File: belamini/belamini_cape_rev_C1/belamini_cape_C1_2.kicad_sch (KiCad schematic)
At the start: 39 parts, among them IC4 TLV320AIC3104, IC5 MIC5317, IC6 USBLC6-2SC6, J2 Conn_01x03, J3 Conn_01x03, J4 Conn_01x03, J5 USB_A, P1 Conn_02x18_Odd_Even, P2 Conn_02x18_Odd_Even

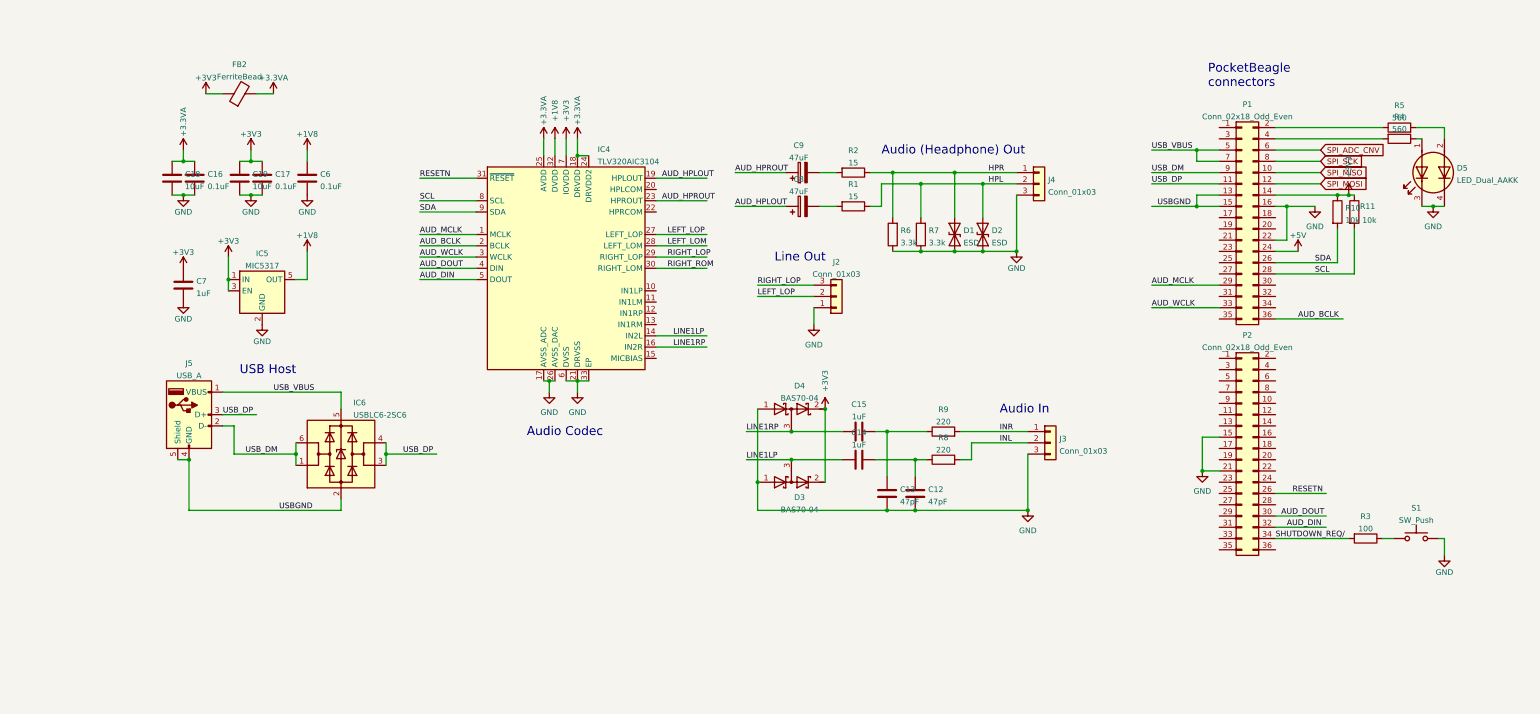
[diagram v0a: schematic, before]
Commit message: Add logo to Mini rev. C1, clean up schematic and add production files
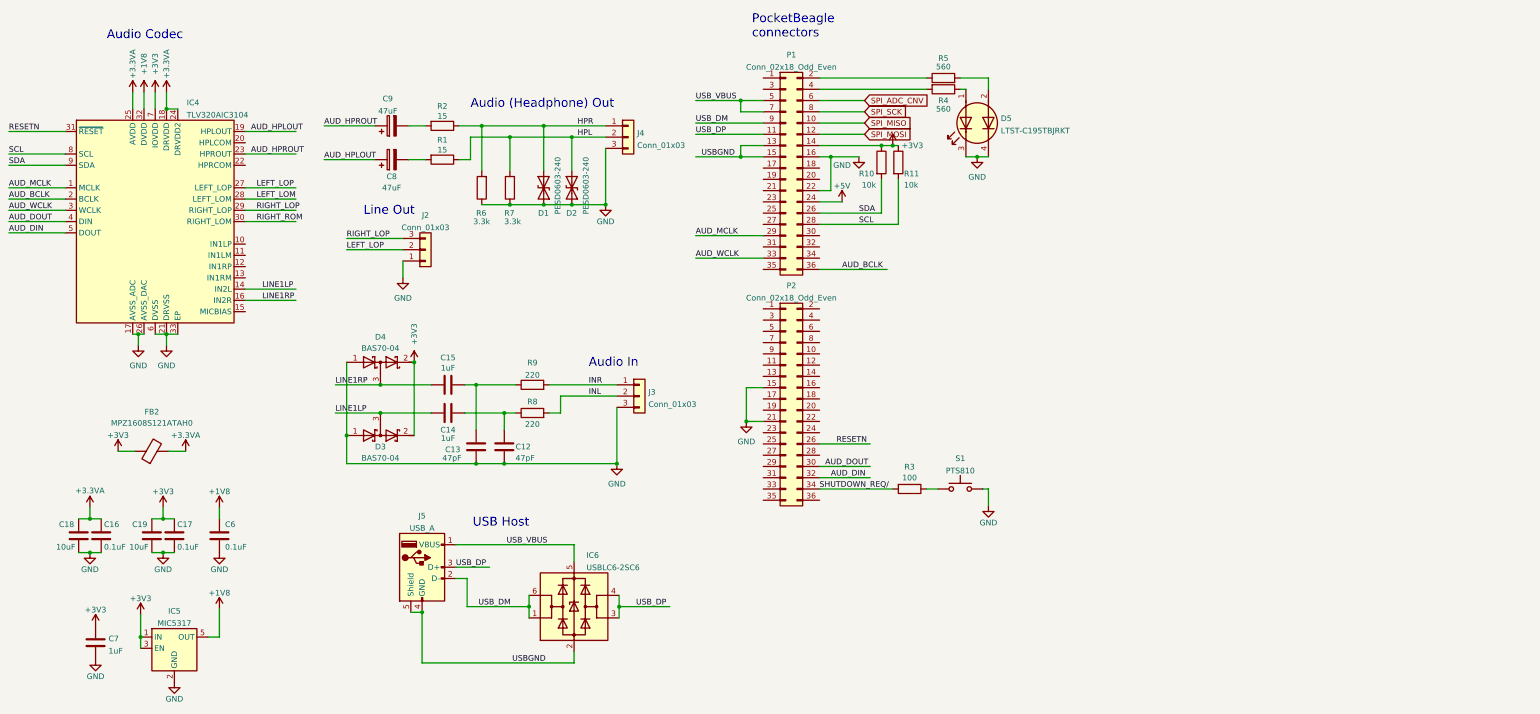
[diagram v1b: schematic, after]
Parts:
- D1, D2: value ESD -> PESD0603-240
- D5: value LED_Dual_AAKK -> LTST-C195TBJRKT
- FB2: value FerriteBead -> MPZ1608S121ATAH0
- S1: value SW_Push -> PTS810
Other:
- company: (none) -> Augmented Instruments Ltd
- title: (none) -> Bela Mini
- moved on the sheet: C12, C13, C14, C15, C16, C17, C18, C19, C6, C7, C8, C9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
